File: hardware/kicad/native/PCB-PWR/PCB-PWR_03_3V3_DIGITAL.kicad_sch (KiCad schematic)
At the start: 16 parts, among them U4 LMR604403SRAKR 3V3 AON

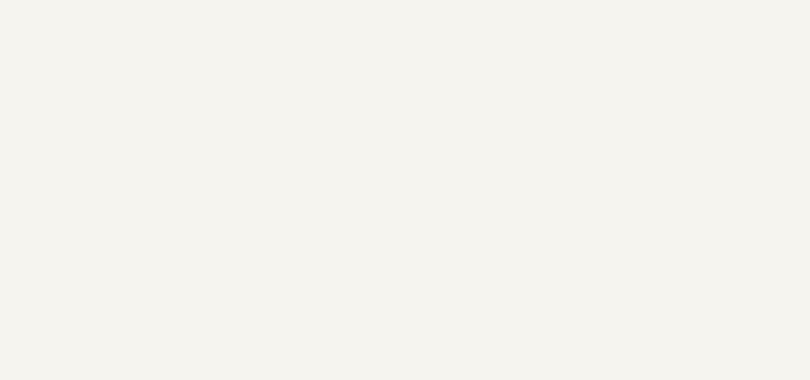
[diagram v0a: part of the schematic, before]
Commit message: pcb-pwr: add local buck input capacitors
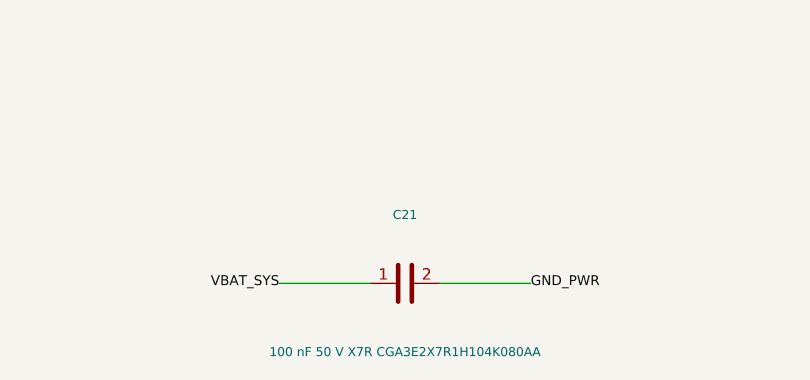
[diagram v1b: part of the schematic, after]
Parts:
- added C21: 100 nF 50 V X7R CGA3E2X7R1H104K080AA, Capacitor_SMD:C_0603_1608Metric, symbol Device:C
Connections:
- net GND_PWR: now also C21.2
- net VBAT_SYS: now also C21.1
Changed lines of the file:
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@@
   (title_block
     (title "Dioneya EVT-PRE-20 PCB-PWR Rev.A - 3V3 digital rail")
-    (date "2026-09-16")
+    (date "2026-09-17")
     (rev "A")
     (company "Dioneya / ZS-BPLA")
@@
     (stroke (width 0.0))
   )
+  (wire (pts (xy 153.67 238.76) (xy 143.51 238.76))
+    (stroke (width 0.0))
+  )
+  (wire (pts (xy 161.29 238.76) (xy 171.45 238.76))
+    (stroke (width 0.0))
+  )
   (wire (pts (xy 153.67 99.06) (xy 143.51 99.06))
     (stroke (width 0.0))
@@
     (effects (font (size 1.1 1.1)))
   )
+  (label "VBAT_SYS" (at 143.51 238.76 180)
+    (effects (font (size 1.1 1.1)))
+  )
+  (label "GND_PWR" (at 171.45 238.76 0)
+    (effects (font (size 1.1 1.1)))
+  )
   (label "3V3_DIGITAL" (at 143.51 99.06 180)
     (effects (font (size 1.1 1.1)))
@@
         )
       )
+    )
+  )
+  (symbol (lib_id "Device:C") (at 157.48 238.76 90) (unit 1)
+    (in_bom yes) (on_board yes) (dnp no)
+    (property "Reference" "C21" (id 0) (at 157.48 231.14 270)
+      (effects (font (size 1.0 1.0)))
+    )
+    (property "Value" "100 nF 50 V X7R CGA3E2X7R1H104K080AA" (id 1) (at 157.48 246.38 270)
+      (effects (font (size 1.0 1.0)))
+    )
+    (property "Footprint" "Capacitor_SMD:C_0603_1608Metric" (id 2) (at 157.48 247.76 0)
+      (effects (font (size 1 1)) hide)
+    )
+    (property "Datasheet" "TDK exact product data for CGA3E2X7R1H104K080AA" (id 3) (at 157.48 249.76 0)
+      (effects (font (size 1 1)) hide)
+    )
+    (pin "1")
+    (pin "2")
+    (instances
+      (project "PCB-PWR"
+        (path "/630df535-af27-5a6d-b3fe-890f0243b40c/88c96396-146a-566a-b60e-947667bc702e"
+          (reference "C21") (unit 1)
+        )
+      )

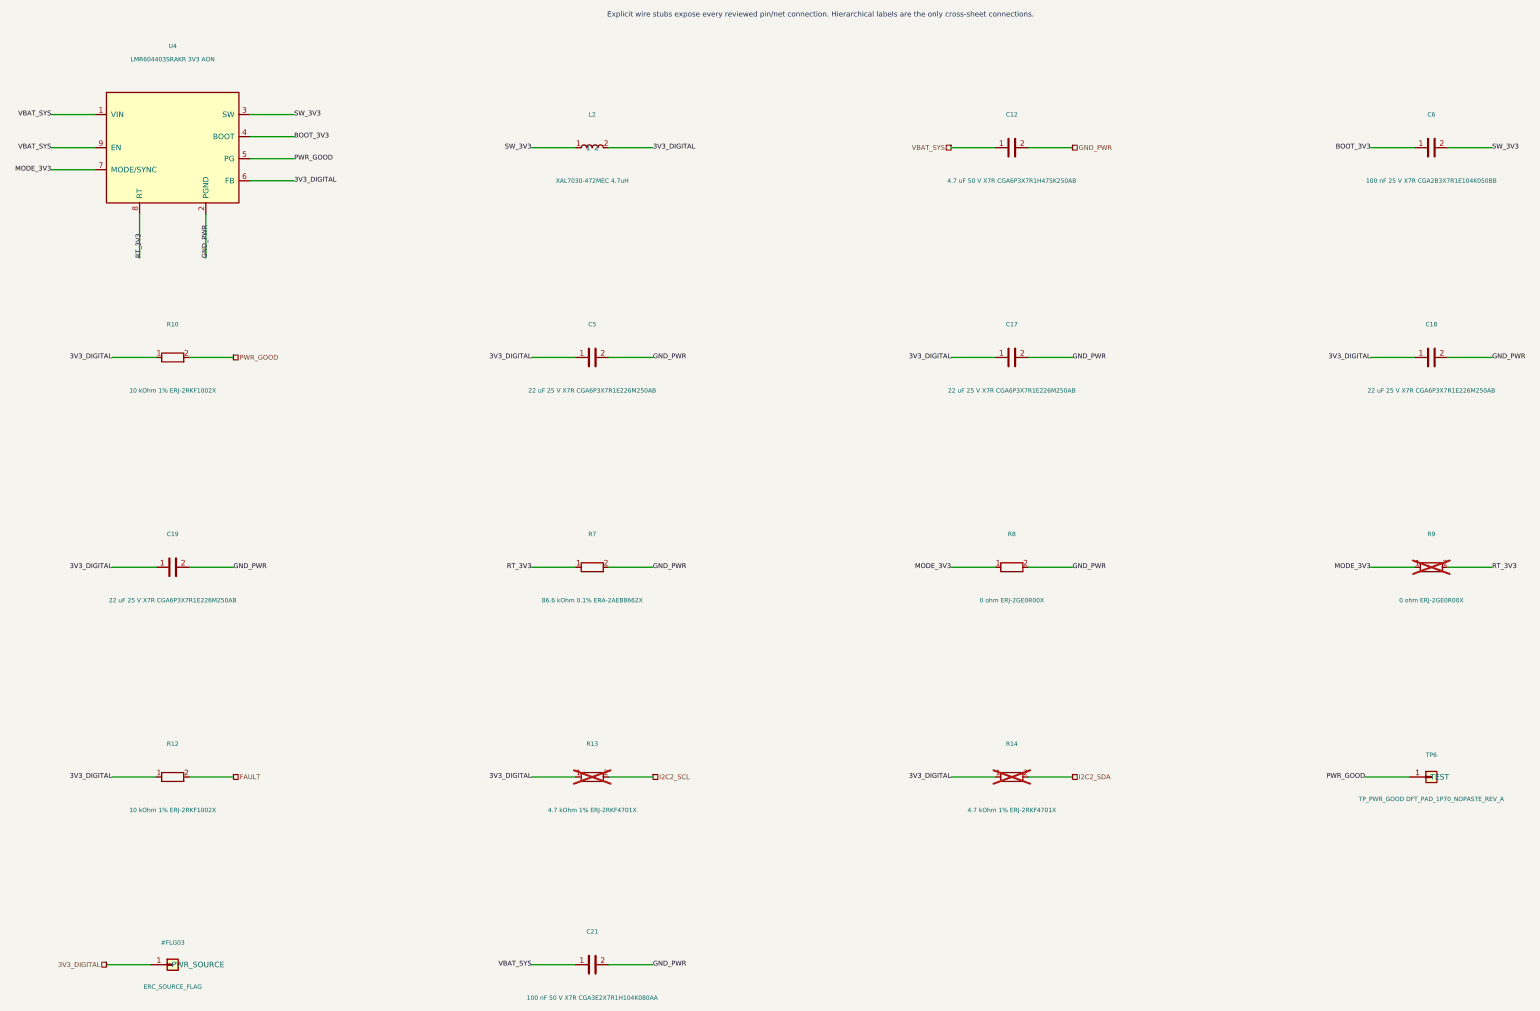
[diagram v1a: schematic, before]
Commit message: pcb-pwr: keep labels clear of connection wires
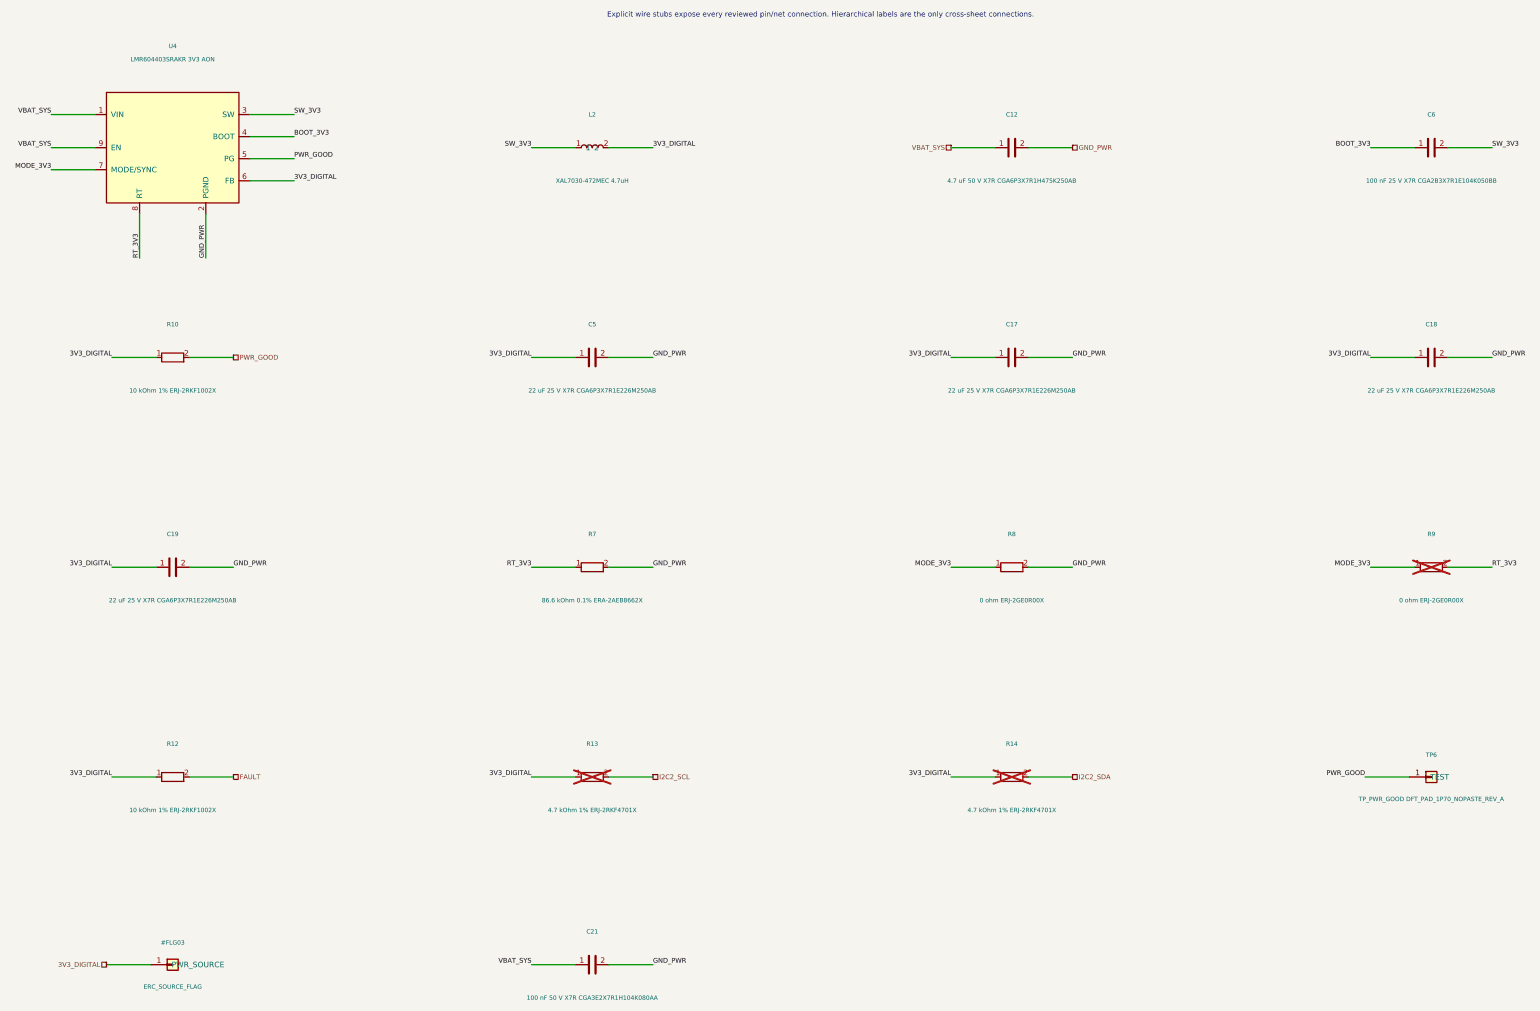
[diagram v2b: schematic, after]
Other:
- title: Dioneya EVT-PRE-20 PCB-PWR Rev.A - 3V3 digital rail -> 3V3 AON rail
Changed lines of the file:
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@@
   (paper "A3")
   (title_block
-    (title "Dioneya EVT-PRE-20 PCB-PWR Rev.A - 3V3 digital rail")
+    (title "3V3 AON rail")
     (date "2026-09-17")
     (rev "A")
@@
   )
   (label "3V3_DIGITAL" (at 240.03 99.06 180)
-    (effects (font (size 1.1 1.1)))
+    (effects (font (size 1.1 1.1)) (justify bottom))
   )
   (label "GND_PWR" (at 267.97 99.06 0)
-    (effects (font (size 1.1 1.1)))
+    (effects (font (size 1.1 1.1)) (justify bottom))
   )
   (label "3V3_DIGITAL" (at 336.55 99.06 180)
-    (effects (font (size 1.1 1.1)))
+    (effects (font (size 1.1 1.1)) (justify bottom))
   )
   (label "GND_PWR" (at 364.49 99.06 0)
-    (effects (font (size 1.1 1.1)))
+    (effects (font (size 1.1 1.1)) (justify bottom))
   )
   (label "3V3_DIGITAL" (at 46.99 147.32 180)
-    (effects (font (size 1.1 1.1)))
+    (effects (font (size 1.1 1.1)) (justify bottom))
   )
   (label "GND_PWR" (at 74.93 147.32 0)
-    (effects (font (size 1.1 1.1)))
+    (effects (font (size 1.1 1.1)) (justify bottom))
   )
   (label "VBAT_SYS" (at 143.51 238.76 180)
-    (effects (font (size 1.1 1.1)))
+    (effects (font (size 1.1 1.1)) (justify bottom))
   )
   (label "GND_PWR" (at 171.45 238.76 0)
-    (effects (font (size 1.1 1.1)))
+    (effects (font (size 1.1 1.1)) (justify bottom))
   )
   (label "3V3_DIGITAL" (at 143.51 99.06 180)
-    (effects (font (size 1.1 1.1)))
+    (effects (font (size 1.1 1.1)) (justify bottom))
   )
   (label "GND_PWR" (at 171.45 99.06 0)
-    (effects (font (size 1.1 1.1)))
+    (effects (font (size 1.1 1.1)) (justify bottom))
   )
   (label "BOOT_3V3" (at 336.55 50.8 180)
-    (effects (font (size 1.1 1.1)))
+    (effects (font (size 1.1 1.1)) (justify bottom))
   )
   (label "SW_3V3" (at 364.49 50.8 0)
-    (effects (font (size 1.1 1.1)))
+    (effects (font (size 1.1 1.1)) (justify bottom))
   )
   (label "SW_3V3" (at 143.51 50.8 180)
-    (effects (font (size 1.1 1.1)))
+    (effects (font (size 1.1 1.1)) (justify bottom))
   )
   (label "3V3_DIGITAL" (at 171.45 50.8 0)
-    (effects (font (size 1.1 1.1)))
+    (effects (font (size 1.1 1.1)) (justify bottom))
   )
   (label "3V3_DIGITAL" (at 46.99 99.06 180)
-    (effects (font (size 1.1 1.1)))
+    (effects (font (size 1.1 1.1)) (justify bottom))
   )
   (label "3V3_DIGITAL" (at 46.99 195.58 180)
-    (effects (font (size 1.1 1.1)))
+    (effects (font (size 1.1 1.1)) (justify bottom))
   )
   (label "3V3_DIGITAL" (at 143.51 195.58 180)
-    (effects (font (size 1.1 1.1)))
+    (effects (font (size 1.1 1.1)) (justify bottom))
   )
   (label "3V3_DIGITAL" (at 240.03 195.58 180)
-    (effects (font (size 1.1 1.1)))
+    (effects (font (size 1.1 1.1)) (justify bottom))
   )
   (label "RT_3V3" (at 143.51 147.32 180)
-    (effects (font (size 1.1 1.1)))
+    (effects (font (size 1.1 1.1)) (justify bottom))
   )
   (label "GND_PWR" (at 171.45 147.32 0)
-    (effects (font (size 1.1 1.1)))
+    (effects (font (size 1.1 1.1)) (justify bottom))
   )
   (label "MODE_3V3" (at 240.03 147.32 180)
-    (effects (font (size 1.1 1.1)))
+    (effects (font (size 1.1 1.1)) (justify bottom))
   )
   (label "GND_PWR" (at 267.97 147.32 0)
-    (effects (font (size 1.1 1.1)))
+    (effects (font (size 1.1 1.1)) (justify bottom))
   )
   (label "MODE_3V3" (at 336.55 147.32 180)
-    (effects (font (size 1.1 1.1)))
+    (effects (font (size 1.1 1.1)) (justify bottom))
   )
   (label "RT_3V3" (at 364.49 147.32 0)
-    (effects (font (size 1.1 1.1)))
+    (effects (font (size 1.1 1.1)) (justify bottom))
   )
   (label "PWR_GOOD" (at 335.28 195.58 180)
-    (effects (font (size 1.1 1.1)))
+    (effects (font (size 1.1 1.1)) (justify bottom))
   )
   (label "VBAT_SYS" (at 33.02 43.18 180)
-    (effects (font (size 1.1 1.1)))
+    (effects (font (size 1.1 1.1)) (justify bottom))
   )
   (label "GND_PWR" (at 68.58 76.2 90)
-    (effects (font (size 1.1 1.1)))
+    (effects (font (size 1.1 1.1)) (justify bottom))
   )
   (label "SW_3V3" (at 88.9 43.18 0)
-    (effects (font (size 1.1 1.1)))
+    (effects (font (size 1.1 1.1)) (justify bottom))
   )
   (label "BOOT_3V3" (at 88.9 48.26 0)
-    (effects (font (size 1.1 1.1)))
+    (effects (font (size 1.1 1.1)) (justify bottom))
   )
   (label "PWR_GOOD" (at 88.9 53.34 0)
-    (effects (font (size 1.1 1.1)))
+    (effects (font (size 1.1 1.1)) (justify bottom))
   )
   (label "3V3_DIGITAL" (at 88.9 58.42 0)
-    (effects (font (size 1.1 1.1)))
+    (effects (font (size 1.1 1.1)) (justify bottom))
   )
   (label "MODE_3V3" (at 33.02 55.88 180)
-    (effects (font (size 1.1 1.1)))
+    (effects (font (size 1.1 1.1)) (justify bottom))
   )
   (label "RT_3V3" (at 53.34 76.2 90)
-    (effects (font (size 1.1 1.1)))
+    (effects (font (size 1.1 1.1)) (justify bottom))
   )
   (label "VBAT_SYS" (at 33.02 50.8 180)
-    (effects (font (size 1.1 1.1)))
+    (effects (font (size 1.1 1.1)) (justify bottom))
   )
   (hierarchical_label "3V3_DIGITAL" (shape passive) (at 45.72 238.76 180)
-    (effects (font (size 1.1 1.1)))
+    (effects (font (size 1.1 1.1)) (justify bottom))
   )
   (hierarchical_label "VBAT_SYS" (shape passive) (at 240.03 50.8 180)
-    (effects (font (size 1.1 1.1)))
+    (effects (font (size 1.1 1.1)) (justify bottom))
   )
   (hierarchical_label "GND_PWR" (shape passive) (at 267.97 50.8 0)
-    (effects (font (size 1.1 1.1)))
+    (effects (font (size 1.1 1.1)) (justify bottom))
   )
   (hierarchical_label "PWR_GOOD" (shape passive) (at 74.93 99.06 0)
-    (effects (font (size 1.1 1.1)))
+    (effects (font (size 1.1 1.1)) (justify bottom))
   )
   (hierarchical_label "FAULT" (shape passive) (at 74.93 195.58 0)
-    (effects (font (size 1.1 1.1)))
+    (effects (font (size 1.1 1.1)) (justify bottom))
   )
   (hierarchical_label "I2C2_SCL" (shape passive) (at 171.45 195.58 0)
-    (effects (font (size 1.1 1.1)))
+    (effects (font (size 1.1 1.1)) (justify bottom))
   )
   (hierarchical_label "I2C2_SDA" (shape passive) (at 267.97 195.58 0)
-    (effects (font (size 1.1 1.1)))
+    (effects (font (size 1.1 1.1)) (justify bottom))
   )
   (symbol (lib_id "DioneyaPWR:ERC_SOURCE_FLAG") (at 60.96 238.76 0) (unit 1)
